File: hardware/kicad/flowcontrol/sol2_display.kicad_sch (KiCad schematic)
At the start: 1 part, among them U2 SOL2_DISP

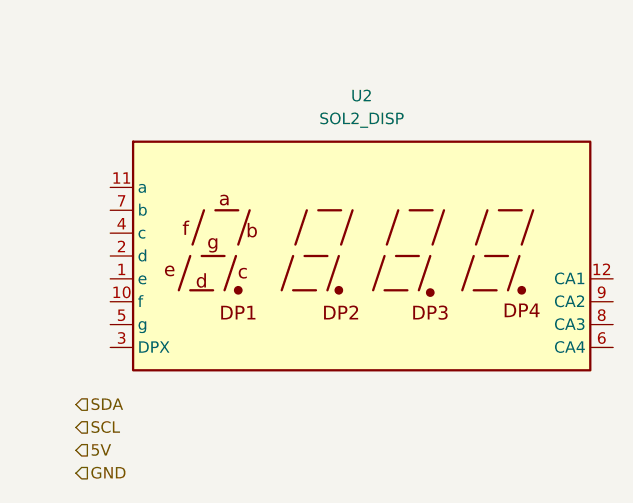
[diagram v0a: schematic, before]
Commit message: Added Arduino coding
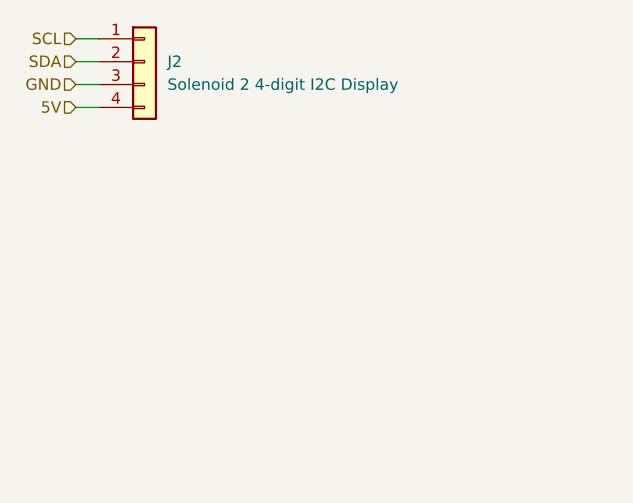
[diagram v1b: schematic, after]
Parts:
- removed U2: SOL2_DISP, Display_7Segment:CA56-12SRWA, symbol Display_Character:CA56-12SRWA
- added J2: Solenoid 2 4-digit I2C Display, symbol Connector_Generic:Conn_01x04
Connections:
- net 5V: now also J2.4 (Pin_4)
- net GND: now also J2.3 (Pin_3)
- net SCL: now also J2.1 (Pin_1)
- net SDA: now also J2.2 (Pin_2)
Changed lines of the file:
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@@
 	(generator_version "8.0")
 	(paper "A5")
-	(hierarchical_label "5V"
+	(wire
+		(pts
+			(xy 27.94 29.21) (xy 25.4 29.21)
+		)
+		(stroke
+			(width 0)
+			(type default)
+		)
+	)
+	(wire
+		(pts
+			(xy 27.94 26.67) (xy 25.4 26.67)
+		)
+		(stroke
+			(width 0)
+			(type default)
+		)
+	)
+	(wire
+		(pts
+			(xy 27.94 31.75) (xy 25.4 31.75)
+		)
+		(stroke
+			(width 0)
+			(type default)
+		)
+	)
+	(wire
+		(pts
+			(xy 27.94 24.13) (xy 25.4 24.13)
+		)
+		(stroke
+			(width 0)
+			(type default)
+		)
+	)
+	(hierarchical_label "SDA"
 		(shape input)
-		(at 25.4 69.85 0)
+		(at 25.4 26.67 180)
 		(fields_autoplaced yes)
 		(effects
@@
 				(size 1.27 1.27)
 			)
-			(justify left)
+			(justify right)
 		)
 	)
-	(hierarchical_label "GND"
+	(hierarchical_label "5V"
 		(shape input)
-		(at 25.4 72.39 0)
+		(at 25.4 31.75 180)
 		(fields_autoplaced yes)
 		(effects
@@
 				(size 1.27 1.27)
 			)
-			(justify left)
+			(justify right)
 		)
 	)
-	(hierarchical_label "SDA"
+	(hierarchical_label "GND"
 		(shape input)
-		(at 25.4 64.77 0)
+		(at 25.4 29.21 180)
 		(fields_autoplaced yes)
 		(effects
@@
 				(size 1.27 1.27)
 			)
-			(justify left)
+			(justify right)
 		)
 	)
 	(hierarchical_label "SCL"
 		(shape input)
-		(at 25.4 67.31 0)
+		(at 25.4 24.13 180)
 		(fields_autoplaced yes)
 		(effects
@@
 				(size 1.27 1.27)
 			)
-			(justify left)
+			(justify right)
 		)
 	)
 	(symbol
-		(lib_id "Display_Character:CA56-12SRWA")
-		(at 57.15 48.26 0)
+		(lib_id "Connector_Generic:Conn_01x04")
+		(at 33.02 26.67 0)
 		(unit 1)
 		(exclude_from_sim no)
@@
 		(dnp no)
 		(fields_autoplaced yes)
-		(property "Reference" "U2"
-			(at 57.15 30.48 0)
+		(property "Reference" "J2"
+			(at 35.56 26.6699 0)
 			(effects
 				(font
 					(size 1.27 1.27)
 				)
+				(justify left)
 			)
 		)
-		(property "Value" "SOL2_DISP"
-			(at 57.15 33.02 0)
+		(property "Value" "Solenoid 2 4-digit I2C Display"
+			(at 35.56 29.2099 0)
 			(effects
 				(font
 					(size 1.27 1.27)
 				)
+				(justify left)
 			)
 		)
-		(property "Footprint" "Display_7Segment:CA56-12SRWA"
-			(at 57.15 63.5 0)
+		(property "Footprint" ""
+			(at 33.02 26.67 0)
 			(effects
 				(font
@@
 			)
 		)
-		(property "Datasheet" "http://www.kingbrightusa.com/images/catalog/SPEC/CA56-12SRWA.pdf"
-			(at 46.228 47.498 0)
+		(property "Datasheet" "~"
+			(at 33.02 26.67 0)
 			(effects
 				(font
@@
 			)
 		)
-		(property "Description" "4 digit 7 segment super bright red LED, common anode"
-			(at 57.15 48.26 0)
+		(property "Description" "Generic connector, single row, 01x04, script generated (kicad-library-utils/schlib/autogen/connector/)"
+			(at 33.02 26.67 0)
 			(effects
 				(font
@@
 			)
 		)
-		(pin "11"
+		(pin "3"
 		)
-		(pin "2"
-		)
-		(pin "5"
-		)
-		(pin "9"
-		)
-		(pin "12"
+		(pin "1"
 		)
 		(pin "4"
 		)
-		(pin "8"
-		)
-		(pin "1"
-		)
-		(pin "3"
-		)
-		(pin "7"
-		)
-		(pin "10"
-		)
-		(pin "6"
+		(pin "2"
 		)
 		(instances
 			(project "flowcontrol"
 				(path "/c8fb4b8d-0361-4798-b029-ef8709a5481b/ff65343e-e678-4d54-acd4-5f7145ef73fd"
-					(reference "U2")
+					(reference "J2")
 					(unit 1)
 				)
